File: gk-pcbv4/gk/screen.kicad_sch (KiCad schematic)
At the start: 16 parts, among them J8 Conn_01x40, J9 Conn_01x06, U12 TPS61165DBV, U13 SN74AVC32T245NMJR

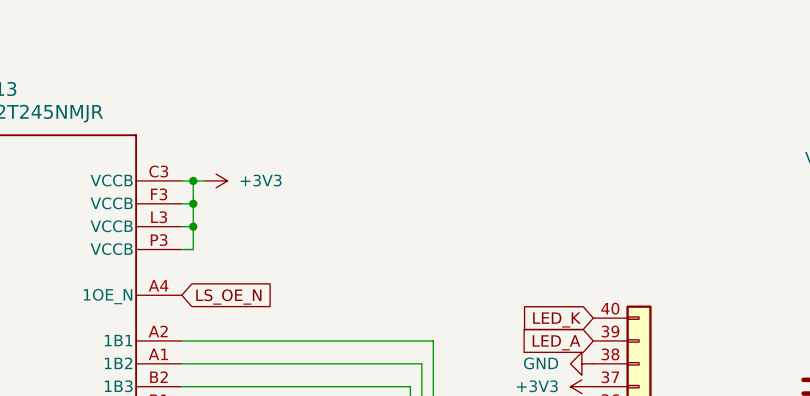
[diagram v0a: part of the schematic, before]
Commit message: update silkscreen text
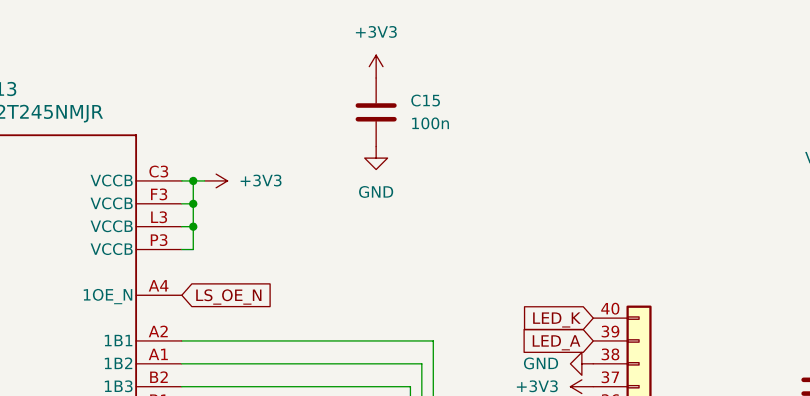
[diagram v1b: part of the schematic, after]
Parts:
- added C15: 100n, Capacitor_SMD:C_0603_1608Metric, symbol Device:C
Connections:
- net +3V3: now also C15.1
- net GND: now also C15.2
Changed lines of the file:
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@@
+	)
+	(symbol
+		(lib_id "Device:C")
+		(at 138.43 25.4 0)
+		(unit 1)
+		(exclude_from_sim no)
+		(in_bom yes)
+		(on_board yes)
+		(dnp no)
+		(fields_autoplaced yes)
+		(property "Reference" "C15"
+			(at 142.24 24.1299 0)
+			(effects
+				(font
+					(size 1.27 1.27)
+				)
+				(justify left)
+			)
+		)
+		(property "Value" "100n"
+			(at 142.24 26.6699 0)
+			(effects
+				(font
+					(size 1.27 1.27)
+				)
+				(justify left)
+			)
+		)
+		(property "Footprint" "Capacitor_SMD:C_0603_1608Metric"
+			(at 139.3952 29.21 0)
+			(effects
+				(font
+					(size 1.27 1.27)
+				)
+				(hide yes)
+			)
+		)
+		(property "Datasheet" "~"
+			(at 138.43 25.4 0)
+			(effects
+				(font
+					(size 1.27 1.27)
+				)
+				(hide yes)
+			)
+		)
+		(property "Description" "Unpolarized capacitor"
+			(at 138.43 25.4 0)
+			(effects
+				(font
+					(size 1.27 1.27)
+				)
+				(hide yes)
+			)
+		)
+		(pin "2"
+		)
+		(pin "1"
+		)
+		(instances
+			(project "gk"
+				(path "/a049c72e-5361-408c-ab21-661d491fee9d/75c00117-6269-4910-8733-11a5b282a070"
+					(reference "C15")
+					(unit 1)
+				)
+			)
+		)
 	)
 	(symbol
@@
 	)
 	(symbol
+		(lib_id "power:GND")
+		(at 138.43 29.21 0)
+		(mirror y)
+		(unit 1)
+		(exclude_from_sim no)
+		(in_bom yes)
+		(on_board yes)
+		(dnp no)
+		(fields_autoplaced yes)
+		(property "Reference" "#PWR093"
+			(at 138.43 35.56 0)
+			(effects
+				(font
+					(size 1.27 1.27)
+				)
+				(hide yes)
+			)
+		)
+		(property "Value" "GND"
+			(at 138.43 34.29 0)
+			(effects
+				(font
+					(size 1.27 1.27)
+				)
+			)
+		)
+		(property "Footprint" ""
+			(at 138.43 29.21 0)
+			(effects
+				(font
+					(size 1.27 1.27)
+				)
+				(hide yes)
+			)
+		)
+		(property "Datasheet" ""
+			(at 138.43 29.21 0)
+			(effects
+				(font
+					(size 1.27 1.27)
+				)
+				(hide yes)
+			)
+		)
+		(property "Description" "Power symbol creates a global label with name \"GND\" , ground"
+			(at 138.43 29.21 0)
+			(effects
+				(font
+					(size 1.27 1.27)
+				)
+				(hide yes)
+			)
+		)
+		(pin "1"
+		)
+		(instances
+			(project "gk"
+				(path "/a049c72e-5361-408c-ab21-661d491fee9d/75c00117-6269-4910-8733-11a5b282a070"
+					(reference "#PWR093")
+					(unit 1)
+				)
+			)
+		)
+	)
+	(symbol
 		(lib_id "Device:R")
 		(at 234.95 148.59 0)
@@
 					(unit 1)
 				)
+			)
+		)
+	)
+	(symbol
+		(lib_id "power:+3V3")
+		(at 138.43 21.59 0)
+		(unit 1)
+		(exclude_from_sim no)
+		(in_bom yes)
+		(on_board yes)
+		(dnp no)
+		(fields_autoplaced yes)
+		(property "Reference" "#PWR090"
+			(at 138.43 25.4 0)
+			(effects
+				(font
+					(size 1.27 1.27)
+				)
+				(hide yes)
+			)
+		)
+		(property "Value" "+3V3"
+			(at 138.43 16.51 0)
+			(effects
+				(font
+					(size 1.27 1.27)
+				)
+			)
+		)
+		(property "Footprint" ""
+			(at 138.43 21.59 0)
+			(effects
+				(font
+					(size 1.27 1.27)
+				)
+				(hide yes)
+			)
+		)
+		(property "Datasheet" ""
+			(at 138.43 21.59 0)
+			(effects
+				(font
+					(size 1.27 1.27)
+				)
+				(hide yes)
+			)
+		)
+		(property "Description" "Power symbol creates a global label with name \"+3V3\""
+			(at 138.43 21.59 0)
+			(effects
+				(font
+					(size 1.27 1.27)
+				)
+				(hide yes)
+			)
+		)
+		(pin "1"
+		)
+		(instances
+			(project "gk"
+				(path "/a049c72e-5361-408c-ab21-661d491fee9d/75c00117-6269-4910-8733-11a5b282a070"
+					(reference "#PWR090")
+					(unit 1)
+				)

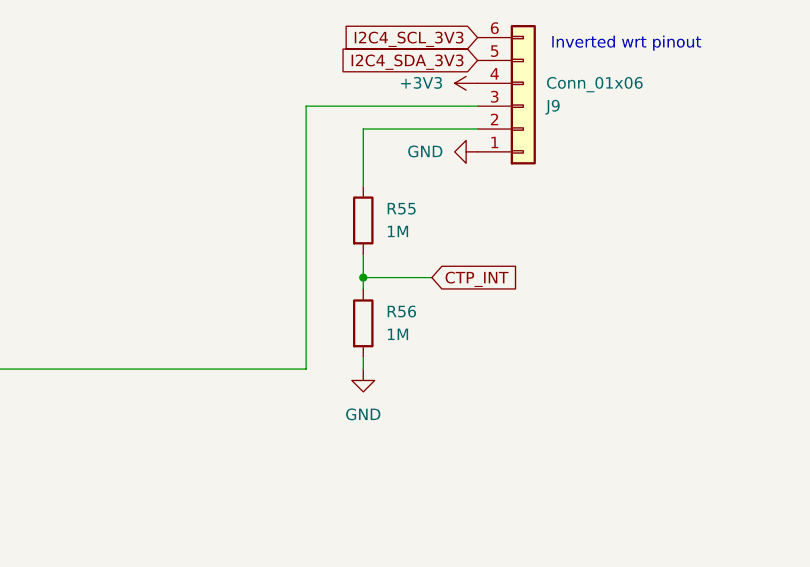
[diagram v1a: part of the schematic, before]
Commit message: update ctp irq resistor divider
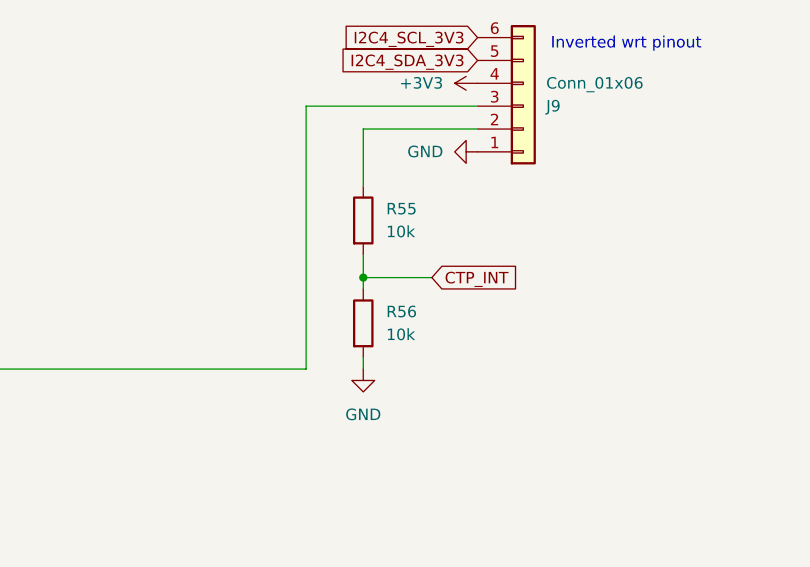
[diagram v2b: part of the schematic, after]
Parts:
- R55, R56: value 1M -> 10k
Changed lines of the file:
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@@
 			)
 		)
-		(property "Value" "1M"
+		(property "Value" "10k"
 			(at 237.49 149.8599 0)
 			(effects
@@
 			)
 		)
-		(property "Value" "1M"
+		(property "Value" "10k"
 			(at 237.49 138.4299 0)
 			(effects

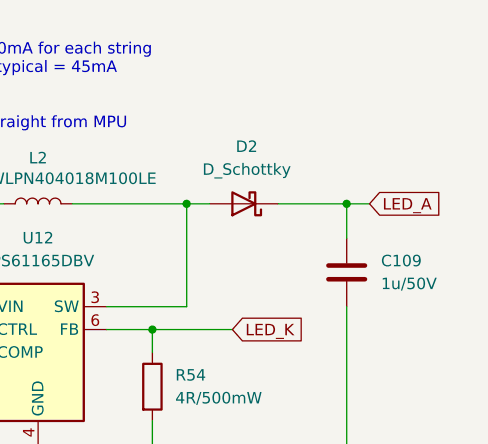
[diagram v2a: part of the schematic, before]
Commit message: add test points to power planes
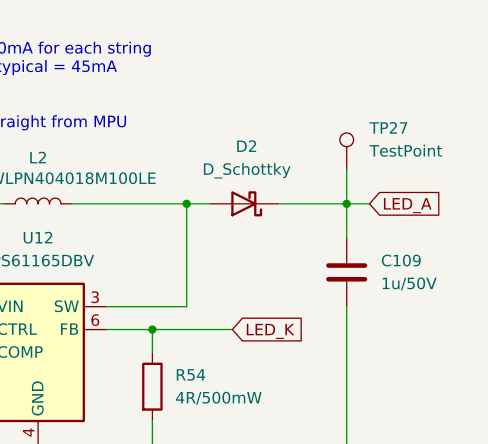
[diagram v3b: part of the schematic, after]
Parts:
- added TP27: TestPoint, TestPoint:TestPoint_Pad_D1.0mm, symbol Connector:TestPoint
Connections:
- net LED_A: now also TP27.1
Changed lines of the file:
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@@
+	(wire
+		(pts
+			(xy 270.51 31.75) (xy 270.51 35.56)
+		)
+		(stroke
+			(width 0)
+			(type default)
+		)
+	)
 	(wire
 		(pts
@@
 					(unit 1)
 				)
+			)
+		)
+	)
+	(symbol
+		(lib_id "Connector:TestPoint")
+		(at 270.51 31.75 0)
+		(unit 1)
+		(exclude_from_sim no)
+		(in_bom yes)
+		(on_board yes)
+		(dnp no)
+		(fields_autoplaced yes)
+		(property "Reference" "TP27"
+			(at 273.05 27.1779 0)
+			(effects
+				(font
+					(size 1.27 1.27)
+				)
+				(justify left)
+			)
+		)
+		(property "Value" "TestPoint"
+			(at 273.05 29.7179 0)
+			(effects
+				(font
+					(size 1.27 1.27)
+				)
+				(justify left)
+			)
+		)
+		(property "Footprint" "TestPoint:TestPoint_Pad_D1.0mm"
+			(at 275.59 31.75 0)
+			(effects
+				(font
+					(size 1.27 1.27)
+				)
+				(hide yes)
+			)
+		)
+		(property "Datasheet" "~"
+			(at 275.59 31.75 0)
+			(effects
+				(font
+					(size 1.27 1.27)
+				)
+				(hide yes)
+			)
+		)
+		(property "Description" "test point"
+			(at 270.51 31.75 0)
+			(effects
+				(font
+					(size 1.27 1.27)
+				)
+				(hide yes)
+			)
+		)
+		(pin "1"
+		)
+		(instances
+			(project "gk"
+				(path "/a049c72e-5361-408c-ab21-661d491fee9d/75c00117-6269-4910-8733-11a5b282a070"
+					(reference "TP27")
+					(unit 1)
+				)
